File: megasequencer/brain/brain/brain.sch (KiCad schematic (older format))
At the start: 9 parts, among them J1 TOP, J2 BOTTOM, J3 Keyboard, J8 RIGHT

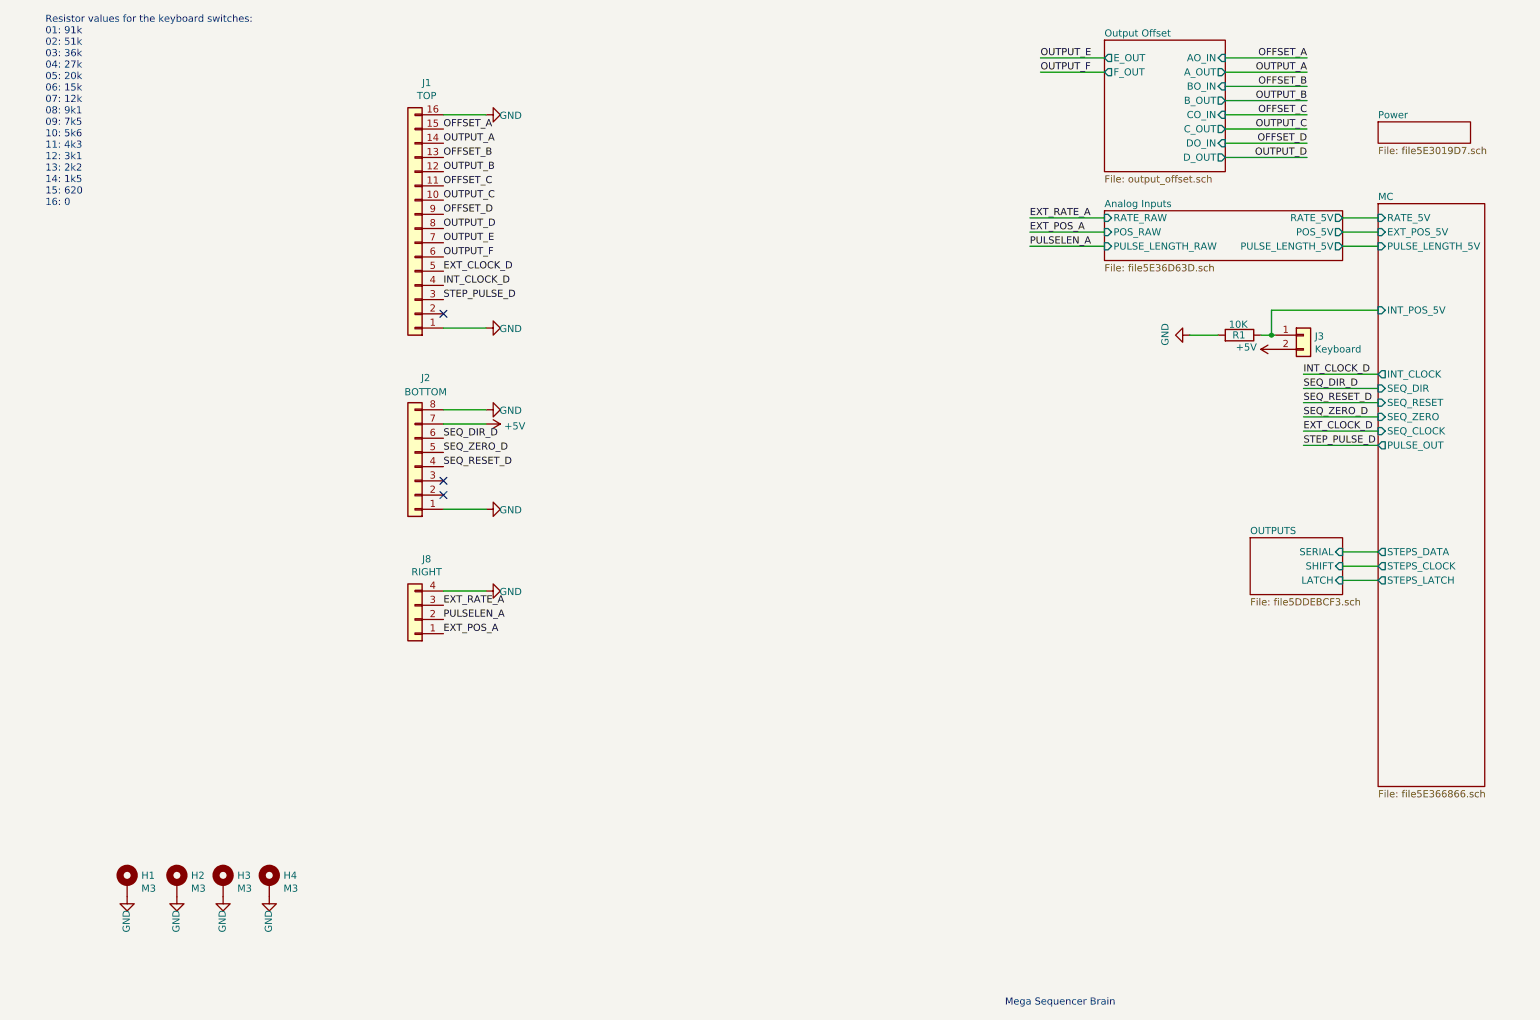
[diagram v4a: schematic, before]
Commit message: Increase trace width on brain, start sorting stuff for vco and start writing shopping list
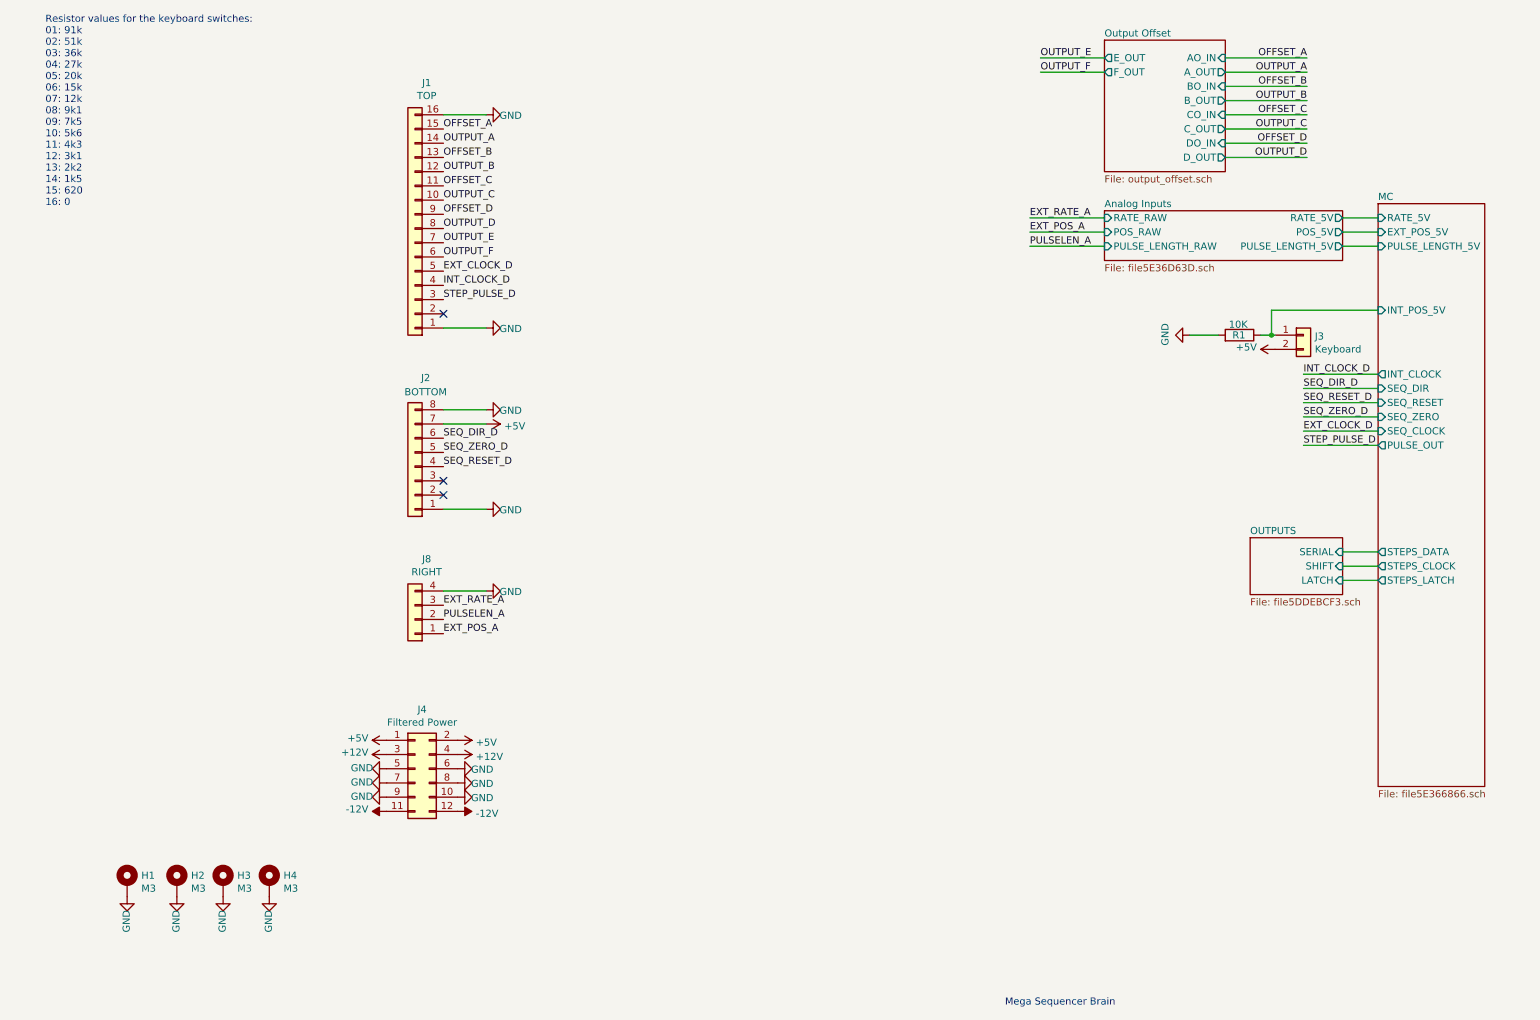
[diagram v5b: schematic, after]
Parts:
- added J4: Filtered Power, Connector_PinHeader_2.54mm:PinHeader_2x06_P2.54mm_Vertical, symbol Connector_Generic:Conn_02x06_Odd_Even
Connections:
- net +5V: now also J4.1 (Pin_1), J4.2 (Pin_2)
- net GND: now also J4.10 (Pin_10), J4.5 (Pin_5), J4.6 (Pin_6), J4.7 (Pin_7), J4.8 (Pin_8), J4.9 (Pin_9)
- new net +12V: J4.3 (Pin_3), J4.4 (Pin_4)
- new net -12V: J4.11 (Pin_11), J4.12 (Pin_12)
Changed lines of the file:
@@
 $Descr A4 11693 8268
 encoding utf-8
-Sheet 1 6
+Sheet 1 5
 Title ""
 Date ""
@@
 Text Notes 7400 7500 0    50   ~ 0
 Mega Sequencer Brain
-$Sheet
-S 10025 1275 650  150
-U 5E3019D8
-F0 "Power" 50
-F1 "file5E3019D7.sch" 50
-$EndSheet
 $Sheet
 S 10025 1850 750  4100
@@
 Wire Wire Line
 	3450 4575 3750 4575
+$Comp
+L Connector_Generic:Conn_02x06_Odd_Even J4
+U 1 1 5E1520BE
+P 3250 5825
+F 0 "J4" H 3300 6242 50  0000 C CNN
+F 1 "Filtered Power" H 3300 6151 50  0000 C CNN
+F 2 "Connector_PinHeader_2.54mm:PinHeader_2x06_P2.54mm_Vertical" H 3250 5825 50  0001 C CNN
+F 3 "~" H 3250 5825 50  0001 C CNN
+	1    3250 5825
+	1    0    0    -1
+$EndComp
+$Comp
+L power:+5V #PWR0103
+U 1 1 5E152D7A
+P 3050 5625
+F 0 "#PWR0103" H 3050 5475 50  0001 C CNN
+F 1 "+5V" V 3065 5753 50  0000 L CNN
+F 2 "" H 3050 5625 50  0001 C CNN
+F 3 "" H 3050 5625 50  0001 C CNN
+	1    3050 5625
+	0    -1   -1   0
+$EndComp
+$Comp
+L power:+5V #PWR0104
+U 1 1 5E153132
+P 3550 5625
+F 0 "#PWR0104" H 3550 5475 50  0001 C CNN
+F 1 "+5V" V 3565 5753 50  0000 L CNN
+F 2 "" H 3550 5625 50  0001 C CNN
+F 3 "" H 3550 5625 50  0001 C CNN
+	1    3550 5625
+	0    1    1    0
+$EndComp
+$Comp
+L power:GND #PWR0105
+U 1 1 5E1535A2
+P 3550 5825
+AR Path="/5E1535A2" Ref="#PWR0105"  Part="1"
+AR Path="/5E353BDD/5E1535A2" Ref="#PWR?"  Part="1"
+F 0 "#PWR0105" H 3550 5575 50  0001 C CNN
+F 1 "GND" V 3555 5652 50  0000 C CNN
+F 2 "" H 3550 5825 50  0001 C CNN
+F 3 "" H 3550 5825 50  0001 C CNN
+	1    3550 5825
+	0    -1   1    0
+$EndComp
+$Comp
+L power:GND #PWR0106
+U 1 1 5E153906
+P 3550 5925
+AR Path="/5E153906" Ref="#PWR0106"  Part="1"
+AR Path="/5E353BDD/5E153906" Ref="#PWR?"  Part="1"
+F 0 "#PWR0106" H 3550 5675 50  0001 C CNN
+F 1 "GND" V 3555 5752 50  0000 C CNN
+F 2 "" H 3550 5925 50  0001 C CNN
+F 3 "" H 3550 5925 50  0001 C CNN
+	1    3550 5925
+	0    -1   1    0
+$EndComp
+$Comp
+L power:GND #PWR0107
+U 1 1 5E153B4C
+P 3550 6025
+AR Path="/5E153B4C" Ref="#PWR0107"  Part="1"
+AR Path="/5E353BDD/5E153B4C" Ref="#PWR?"  Part="1"
+F 0 "#PWR0107" H 3550 5775 50  0001 C CNN
+F 1 "GND" V 3555 5852 50  0000 C CNN
+F 2 "" H 3550 6025 50  0001 C CNN
+F 3 "" H 3550 6025 50  0001 C CNN
+	1    3550 6025
+	0    -1   1    0
+$EndComp
+$Comp
+L power:GND #PWR0108
+U 1 1 5E153DCD
+P 3050 5825
+AR Path="/5E153DCD" Ref="#PWR0108"  Part="1"
+AR Path="/5E353BDD/5E153DCD" Ref="#PWR?"  Part="1"
+F 0 "#PWR0108" H 3050 5575 50  0001 C CNN
+F 1 "GND" V 3055 5652 50  0000 C CNN
+F 2 "" H 3050 5825 50  0001 C CNN
+F 3 "" H 3050 5825 50  0001 C CNN
+	1    3050 5825
+	0    1    -1   0
+$EndComp
+$Comp
+L power:GND #PWR0109
+U 1 1 5E154255
+P 3050 5925
+AR Path="/5E154255" Ref="#PWR0109"  Part="1"
+AR Path="/5E353BDD/5E154255" Ref="#PWR?"  Part="1"
+F 0 "#PWR0109" H 3050 5675 50  0001 C CNN
+F 1 "GND" V 3055 5752 50  0000 C CNN
+F 2 "" H 3050 5925 50  0001 C CNN
+F 3 "" H 3050 5925 50  0001 C CNN
+	1    3050 5925
+	0    1    -1   0
+$EndComp
+$Comp
+L power:GND #PWR0110
+U 1 1 5E1544D5
+P 3050 6025
+AR Path="/5E1544D5" Ref="#PWR0110"  Part="1"
+AR Path="/5E353BDD/5E1544D5" Ref="#PWR?"  Part="1"
+F 0 "#PWR0110" H 3050 5775 50  0001 C CNN
+F 1 "GND" V 3055 5852 50  0000 C CNN
+F 2 "" H 3050 6025 50  0001 C CNN
+F 3 "" H 3050 6025 50  0001 C CNN
+	1    3050 6025
+	0    1    -1   0
+$EndComp
+$Comp
+L power:+12V #PWR0111
+U 1 1 5E154A1C
+P 3550 5725
+F 0 "#PWR0111" H 3550 5575 50  0001 C CNN
+F 1 "+12V" V 3565 5853 50  0000 L CNN
+F 2 "" H 3550 5725 50  0001 C CNN
+F 3 "" H 3550 5725 50  0001 C CNN
+	1    3550 5725
+	0    1    1    0
+$EndComp
+$Comp
+L power:+12V #PWR0112
+U 1 1 5E154DDF
+P 3050 5725
+F 0 "#PWR0112" H 3050 5575 50  0001 C CNN
+F 1 "+12V" V 3065 5853 50  0000 L CNN
+F 2 "" H 3050 5725 50  0001 C CNN
+F 3 "" H 3050 5725 50  0001 C CNN
+	1    3050 5725
+	0    -1   -1   0
+$EndComp
+$Comp
+L power:-12V #PWR0113
+U 1 1 5E155598
+P 3550 6125
+F 0 "#PWR0113" H 3550 6225 50  0001 C CNN
+F 1 "-12V" V 3565 6253 50  0000 L CNN
+F 2 "" H 3550 6125 50  0001 C CNN
+F 3 "" H 3550 6125 50  0001 C CNN
+	1    3550 6125
+	0    1    1    0
+$EndComp
+$Comp
+L power:-12V #PWR0114
+U 1 1 5E15597E
+P 3050 6125
+F 0 "#PWR0114" H 3050 6225 50  0001 C CNN
+F 1 "-12V" V 3065 6253 50  0000 L CNN
+F 2 "" H 3050 6125 50  0001 C CNN
+F 3 "" H 3050 6125 50  0001 C CNN
+	1    3050 6125
+	0    -1   -1   0
+$EndComp
 $EndSCHEMATC
